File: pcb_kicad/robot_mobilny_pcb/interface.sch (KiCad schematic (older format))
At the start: 21 parts, among them SW3 Button_1

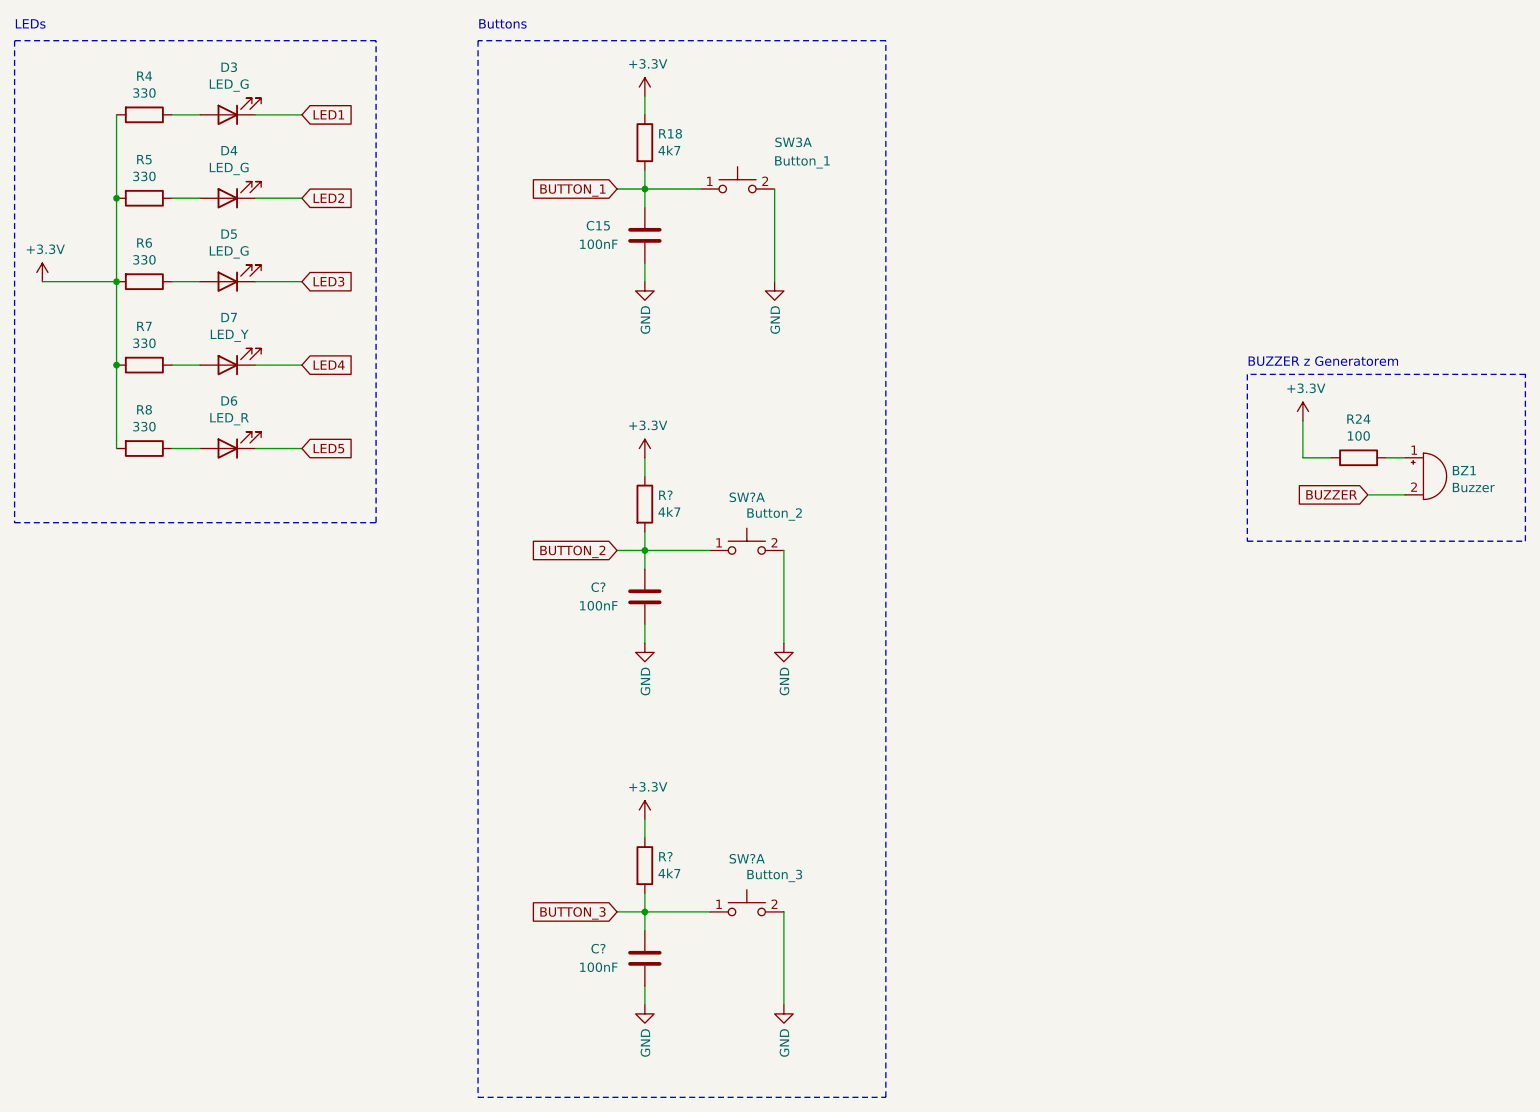
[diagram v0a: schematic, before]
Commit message: schematic update
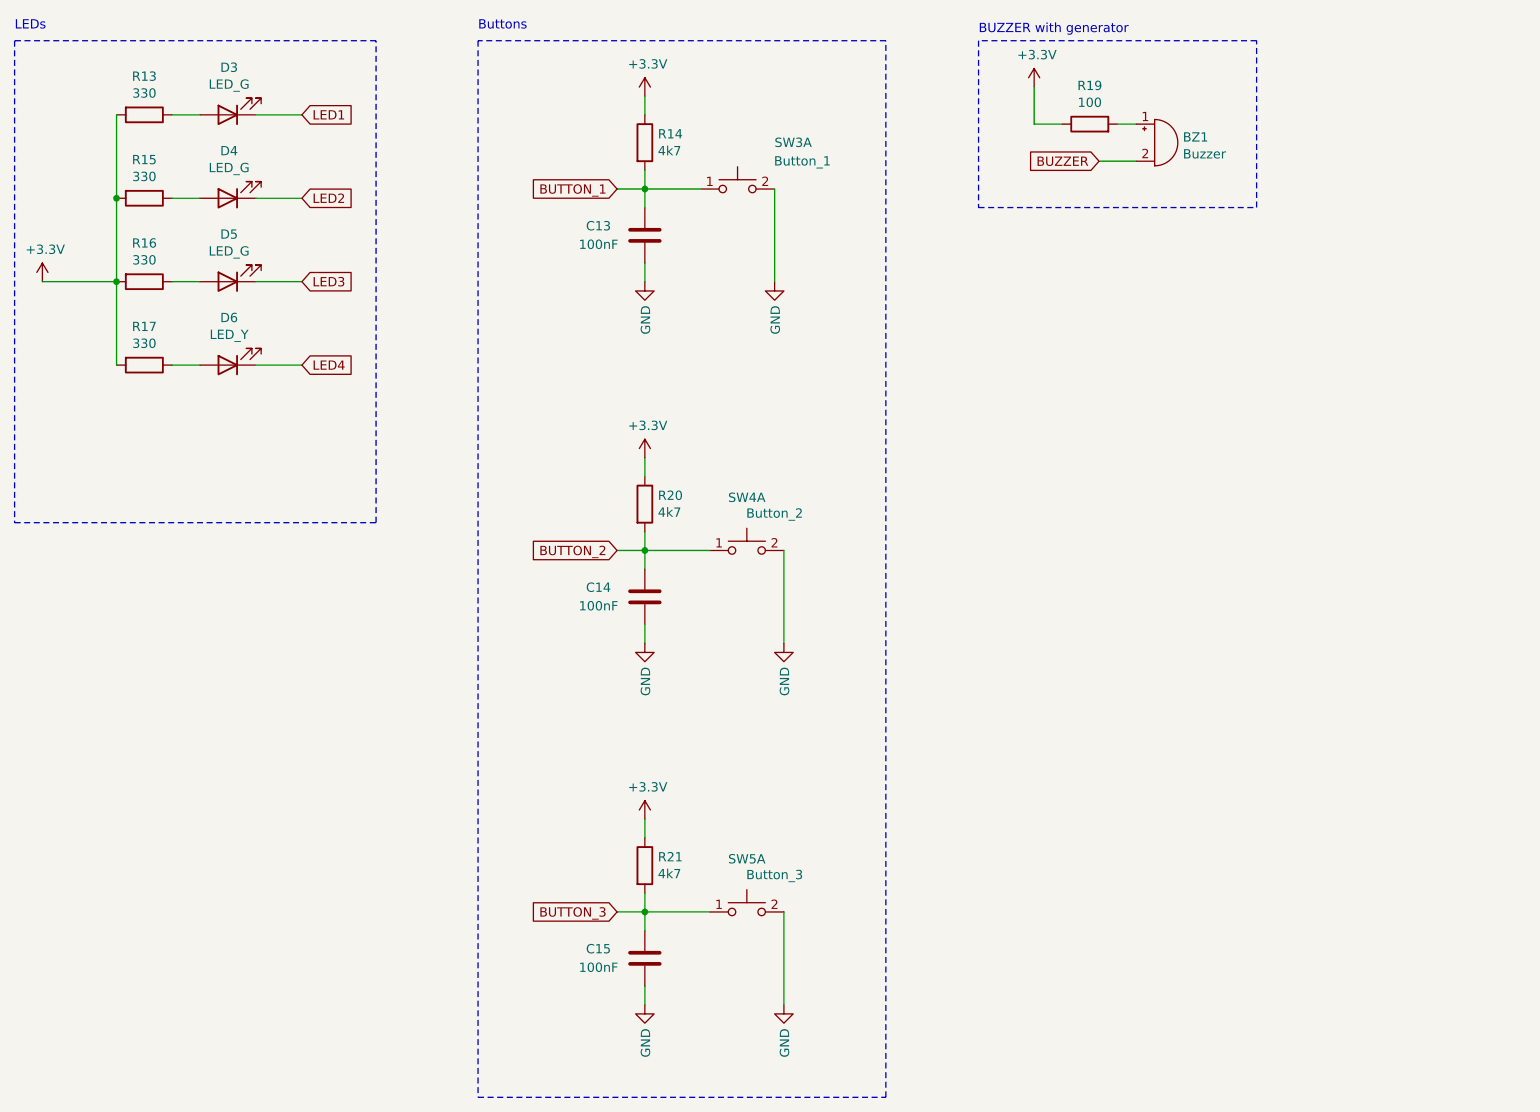
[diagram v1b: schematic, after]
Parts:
- removed D6: LED_R, symbol Device:LED
- removed R8: 330, symbol Device:R
- D3, D4, D5: footprint (none) -> LED_THT:LED_D5.0mm
- D6: renamed from D7; footprint (none) -> LED_THT:LED_D5.0mm
- SW3: footprint (none) -> Button_Switch_THT:SW_PUSH_6mm_H9.5mm
- SW4, SW5: renamed from SW?; footprint (none) -> Button_Switch_THT:SW_PUSH_6mm_H9.5mm
- gave numbers to parts that had none: 4
- renumbered C15 to C13, R4 to R13, R18 to R14, R5 to R15, R6 to R16, R7 to R17, R24 to R19
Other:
- note added: "BUZZER with generator\n\n"
- note removed: "BUZZER z Generatorem\n\n"
- moved on the sheet: BZ1, R19

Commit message: schematic_update
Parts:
- BZ201: renamed from BZ1; footprint (none) -> Buzzer_Beeper:Buzzer_12x9.5RM7.6
- C201: renamed from C13; footprint (none) -> Capacitor_THT:C_Disc_D5.0mm_W2.5mm_P2.50mm
- C202: renamed from C14; footprint (none) -> Capacitor_THT:C_Disc_D5.0mm_W2.5mm_P2.50mm
- C203: renamed from C15; footprint (none) -> Capacitor_THT:C_Disc_D5.0mm_W2.5mm_P2.50mm
- R201: renamed from R13; footprint (none) -> Resistor_THT:R_Axial_DIN0207_L6.3mm_D2.5mm_P10.16mm_Horizontal
- R202: renamed from R19; value 100 -> 330; footprint (none) -> Resistor_THT:R_Axial_DIN0207_L6.3mm_D2.5mm_P10.16mm_Horizontal
- R203: renamed from R14; footprint (none) -> Resistor_THT:R_Axial_DIN0207_L6.3mm_D2.5mm_P10.16mm_Horizontal
- R204: renamed from R15; footprint (none) -> Resistor_THT:R_Axial_DIN0207_L6.3mm_D2.5mm_P10.16mm_Horizontal
- R205: renamed from R16; footprint (none) -> Resistor_THT:R_Axial_DIN0207_L6.3mm_D2.5mm_P10.16mm_Horizontal
- R206: renamed from R17; footprint (none) -> Resistor_THT:R_Axial_DIN0207_L6.3mm_D2.5mm_P10.16mm_Horizontal
- R207: renamed from R20; footprint (none) -> Resistor_THT:R_Axial_DIN0207_L6.3mm_D2.5mm_P10.16mm_Horizontal
- R208: renamed from R21; footprint (none) -> Resistor_THT:R_Axial_DIN0207_L6.3mm_D2.5mm_P10.16mm_Horizontal
- renumbered D3 to D201, D4 to D202, D5 to D203, D6 to D204, SW3 to SW201, SW4 to SW202, SW5 to SW203
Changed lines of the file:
@@
 $EndDescr
 $Comp
-L Device:LED D4
+L Device:LED D202
 U 1 1 617723D4
 P 2600 1950
-F 0 "D4" H 2593 1695 50  0000 C CNN
+F 0 "D202" H 2593 1695 50  0000 C CNN
 F 1 "LED_G" H 2593 1786 50  0000 C CNN
 F 2 "LED_THT:LED_D5.0mm" H 2600 1950 50  0001 C CNN
@@
 $EndComp
 $Comp
-L Device:LED D5
+L Device:LED D203
 U 1 1 61772A27
 P 2600 2400
-F 0 "D5" H 2593 2145 50  0000 C CNN
+F 0 "D203" H 2593 2145 50  0000 C CNN
 F 1 "LED_G" H 2593 2236 50  0000 C CNN
 F 2 "LED_THT:LED_D5.0mm" H 2600 2400 50  0001 C CNN
@@
 $EndComp
 $Comp
-L Device:LED D6
+L Device:LED D204
 U 1 1 61773566
 P 2600 2850
-F 0 "D6" H 2593 2595 50  0000 C CNN
+F 0 "D204" H 2593 2595 50  0000 C CNN
 F 1 "LED_Y" H 2593 2686 50  0000 C CNN
 F 2 "LED_THT:LED_D5.0mm" H 2600 2850 50  0001 C CNN
@@
 $EndComp
 $Comp
-L Device:R R13
+L Device:R R201
 U 1 1 61773BF9
 P 2150 1500
-F 0 "R13" V 1943 1500 50  0000 C CNN
+F 0 "R201" V 1943 1500 50  0000 C CNN
 F 1 "330" V 2034 1500 50  0000 C CNN
-F 2 "" V 2080 1500 50  0001 C CNN
+F 2 "Resistor_THT:R_Axial_DIN0207_L6.3mm_D2.5mm_P10.16mm_Horizontal" V 2080 1500 50  0001 C CNN
 F 3 "~" H 2150 1500 50  0001 C CNN
 	1    2150 1500
@@
 $EndComp
 $Comp
-L Device:R R15
+L Device:R R204
 U 1 1 61774702
 P 2150 1950
-F 0 "R15" V 1943 1950 50  0000 C CNN
+F 0 "R204" V 1943 1950 50  0000 C CNN
 F 1 "330" V 2034 1950 50  0000 C CNN
-F 2 "" V 2080 1950 50  0001 C CNN
+F 2 "Resistor_THT:R_Axial_DIN0207_L6.3mm_D2.5mm_P10.16mm_Horizontal" V 2080 1950 50  0001 C CNN
 F 3 "~" H 2150 1950 50  0001 C CNN
 	1    2150 1950
@@
 $EndComp
 $Comp
-L Device:R R16
+L Device:R R205
 U 1 1 617749A4
 P 2150 2400
-F 0 "R16" V 1943 2400 50  0000 C CNN
+F 0 "R205" V 1943 2400 50  0000 C CNN
 F 1 "330" V 2034 2400 50  0000 C CNN
-F 2 "" V 2080 2400 50  0001 C CNN
+F 2 "Resistor_THT:R_Axial_DIN0207_L6.3mm_D2.5mm_P10.16mm_Horizontal" V 2080 2400 50  0001 C CNN
 F 3 "~" H 2150 2400 50  0001 C CNN
 	1    2150 2400
@@
 $EndComp
 $Comp
-L Device:R R17
+L Device:R R206
 U 1 1 61774CCB
 P 2150 2850
-F 0 "R17" V 1943 2850 50  0000 C CNN
+F 0 "R206" V 1943 2850 50  0000 C CNN
 F 1 "330" V 2034 2850 50  0000 C CNN
-F 2 "" V 2080 2850 50  0001 C CNN
+F 2 "Resistor_THT:R_Axial_DIN0207_L6.3mm_D2.5mm_P10.16mm_Horizontal" V 2080 2850 50  0001 C CNN
 F 3 "~" H 2150 2850 50  0001 C CNN
 	1    2150 2850
@@
 Connection ~ 2000 2400
 $Comp
-L power:+3.3V #PWR028
+L power:+3.3V #PWR0203
 U 1 1 6177600C
 P 1600 2400
-F 0 "#PWR028" H 1600 2250 50  0001 C CNN
+F 0 "#PWR0203" H 1600 2250 50  0001 C CNN
 F 1 "+3.3V" H 1615 2573 50  0000 C CNN
 F 2 "" H 1600 2400 50  0001 C CNN
@@
 	2750 2850 3000 2850
 $Comp
-L Switch:SW_Push_Dual_x2 SW3
+L Switch:SW_Push_Dual_x2 SW201
 U 1 1 6177803B
 P 5350 1900
-F 0 "SW3" H 5650 2150 50  0000 C CNN
+F 0 "SW201" H 5650 2150 50  0000 C CNN
 F 1 "Button_1" H 5700 2050 50  0000 C CNN
 F 2 "Button_Switch_THT:SW_PUSH_6mm_H9.5mm" H 5350 2100 50  0001 C CNN
@@
 $EndComp
 $Comp
-L Device:R R14
+L Device:R R203
 U 1 1 61779C00
 P 4850 1650
-F 0 "R14" H 4920 1696 50  0000 L CNN
+F 0 "R203" H 4920 1696 50  0000 L CNN
 F 1 "4k7" H 4920 1605 50  0000 L CNN
-F 2 "" V 4780 1650 50  0001 C CNN
+F 2 "Resistor_THT:R_Axial_DIN0207_L6.3mm_D2.5mm_P10.16mm_Horizontal" V 4780 1650 50  0001 C CNN
 F 3 "~" H 4850 1650 50  0001 C CNN
 	1    4850 1650
@@
 $EndComp
 $Comp
-L power:+3.3V #PWR027
+L power:+3.3V #PWR0202
 U 1 1 6177B1CB
 P 4850 1400
-F 0 "#PWR027" H 4850 1250 50  0001 C CNN
+F 0 "#PWR0202" H 4850 1250 50  0001 C CNN
 F 1 "+3.3V" H 4865 1573 50  0000 C CNN
 F 2 "" H 4850 1400 50  0001 C CNN
@@
 	4850 1800 4850 1900
 $Comp
-L Device:C C13
+L Device:C C201
 U 1 1 6177C94D
 P 4850 2150
-F 0 "C13" H 5100 2100 50  0000 C CNN
+F 0 "C201" H 5100 2100 50  0000 C CNN
 F 1 "100nF" H 5100 2200 50  0000 C CNN
-F 2 "" H 4888 2000 50  0001 C CNN
+F 2 "Capacitor_THT:C_Disc_D5.0mm_W2.5mm_P2.50mm" H 4888 2000 50  0001 C CNN
 F 3 "~" H 4850 2150 50  0001 C CNN
 	1    4850 2150
@@
 BUTTON_1
 $Comp
-L power:GND #PWR029
+L power:GND #PWR0204
 U 1 1 6177E65E
 P 4850 2400
-F 0 "#PWR029" H 4850 2150 50  0001 C CNN
+F 0 "#PWR0204" H 4850 2150 50  0001 C CNN
 F 1 "GND" V 4855 2272 50  0000 R CNN
 F 2 "" H 4850 2400 50  0001 C CNN
@@
 $EndComp
 $Comp
-L Device:Buzzer BZ1
+L Device:Buzzer BZ201
 U 1 1 61784492
 P 7600 1650
-F 0 "BZ1" H 7752 1679 50  0000 L CNN
+F 0 "BZ201" H 7752 1679 50  0000 L CNN
 F 1 "Buzzer" H 7752 1588 50  0000 L CNN
-F 2 "" V 7575 1750 50  0001 C CNN
+F 2 "Buzzer_Beeper:Buzzer_12x9.5RM7.6" V 7575 1750 50  0001 C CNN
 F 3 "~" V 7575 1750 50  0001 C CNN
 	1    7600 1650
@@
 $EndComp
 $Comp
-L power:+3.3V #PWR031
+L power:+3.3V #PWR0201
 U 1 1 618AE479
 P 6950 1350
-F 0 "#PWR031" H 6950 1200 50  0001 C CNN
+F 0 "#PWR0201" H 6950 1200 50  0001 C CNN
 F 1 "+3.3V" H 6965 1523 50  0000 C CNN
 F 2 "" H 6950 1350 50  0001 C CNN
@@
 	7300 1750 7500 1750
 $Comp
-L Device:R R19
+L Device:R R202
 U 1 1 618B52DF
 P 7250 1550
-F 0 "R19" V 7457 1550 50  0000 C CNN
-F 1 "100" V 7366 1550 50  0000 C CNN
-F 2 "" V 7180 1550 50  0001 C CNN
+F 0 "R202" V 7457 1550 50  0000 C CNN
+F 1 "330" V 7366 1550 50  0000 C CNN
+F 2 "Resistor_THT:R_Axial_DIN0207_L6.3mm_D2.5mm_P10.16mm_Horizontal" V 7180 1550 50  0001 C CNN
 F 3 "~" H 7250 1550 50  0001 C CNN
 	1    7250 1550
@@
 	3400 1100 1450 1100
 $Comp
-L Device:LED D3
+L Device:LED D201
 U 1 1 61771269
 P 2600 1500
-F 0 "D3" H 2593 1245 50  0000 C CNN
+F 0 "D201" H 2593 1245 50  0000 C CNN
 F 1 "LED_G" H 2593 1336 50  0000 C CNN
 F 2 "LED_THT:LED_D5.0mm" H 2600 1500 50  0001 C CNN
@@
 	4850 2300 4850 2400
 $Comp
-L power:GND #PWR030
+L power:GND #PWR0205
 U 1 1 618E5535
 P 5550 2400
-F 0 "#PWR030" H 5550 2150 50  0001 C CNN
+F 0 "#PWR0205" H 5550 2150 50  0001 C CNN
 F 1 "GND" V 5555 2272 50  0000 R CNN
 F 2 "" H 5550 2400 50  0001 C CNN
@@
 BUTTON_3
 $Comp
-L Switch:SW_Push_Dual_x2 SW4
+L Switch:SW_Push_Dual_x2 SW202
 U 1 1 618EB4A2
 P 5400 3850
-F 0 "SW4" H 5400 4135 50  0000 C CNN
+F 0 "SW202" H 5400 4135 50  0000 C CNN
 F 1 "Button_2" H 5550 4050 50  0000 C CNN
 F 2 "Button_Switch_THT:SW_PUSH_6mm_H9.5mm" H 5400 4050 50  0001 C CNN
@@
 $EndComp
 $Comp
-L Device:R R20
+L Device:R R207
 U 1 1 618EB4AE
 P 4850 3600
-F 0 "R20" H 4920 3646 50  0000 L CNN
+F 0 "R207" H 4920 3646 50  0000 L CNN
 F 1 "4k7" H 4920 3555 50  0000 L CNN
-F 2 "" V 4780 3600 50  0001 C CNN
+F 2 "Resistor_THT:R_Axial_DIN0207_L6.3mm_D2.5mm_P10.16mm_Horizontal" V 4780 3600 50  0001 C CNN
 F 3 "~" H 4850 3600 50  0001 C CNN
 	1    4850 3600
@@
 $EndComp
 $Comp
-L power:+3.3V #PWR032
+L power:+3.3V #PWR0206
 U 1 1 618EB4B4
 P 4850 3350
-F 0 "#PWR032" H 4850 3200 50  0001 C CNN
+F 0 "#PWR0206" H 4850 3200 50  0001 C CNN
 F 1 "+3.3V" H 4865 3523 50  0000 C CNN
 F 2 "" H 4850 3350 50  0001 C CNN
@@
 	4850 3750 4850 3850
 $Comp
-L Device:C C14
+L Device:C C202
 U 1 1 618EB4BD
 P 4850 4100
-F 0 "C14" H 5100 4050 50  0000 C CNN
+F 0 "C202" H 5100 4050 50  0000 C CNN
 F 1 "100nF" H 5100 4150 50  0000 C CNN
-F 2 "" H 4888 3950 50  0001 C CNN
+F 2 "Capacitor_THT:C_Disc_D5.0mm_W2.5mm_P2.50mm" H 4888 3950 50  0001 C CNN
 F 3 "~" H 4850 4100 50  0001 C CNN
 	1    4850 4100
@@
 $EndComp
 $Comp
-L power:GND #PWR033
+L power:GND #PWR0207
 U 1 1 618EB4C3
 P 4850 4350
-F 0 "#PWR033" H 4850 4100 50  0001 C CNN
+F 0 "#PWR0207" H 4850 4100 50  0001 C CNN
 F 1 "GND" V 4855 4222 50  0000 R CNN
 F 2 "" H 4850 4350 50  0001 C CNN
@@
 	4850 4250 4850 4350
 $Comp
-L power:GND #PWR034
+L power:GND #PWR0208
 U 1 1 618EB4CD
 P 5600 4350
-F 0 "#PWR034" H 5600 4100 50  0001 C CNN
+F 0 "#PWR0208" H 5600 4100 50  0001 C CNN
 F 1 "GND" V 5605 4222 50  0000 R CNN
 F 2 "" H 5600 4350 50  0001 C CNN
@@
 	5600 3850 5600 4350
 $Comp
-L Switch:SW_Push_Dual_x2 SW5
+L Switch:SW_Push_Dual_x2 SW203
 U 1 1 618EF7CF
 P 5400 5800
-F 0 "SW5" H 5400 6085 50  0000 C CNN
+F 0 "SW203" H 5400 6085 50  0000 C CNN
 F 1 "Button_3" H 5550 6000 50  0000 C CNN
 F 2 "Button_Switch_THT:SW_PUSH_6mm_H9.5mm" H 5400 6000 50  0001 C CNN
@@
 $EndComp
 $Comp
-L Device:R R21
+L Device:R R208
 U 1 1 618EF7DB
 P 4850 5550
-F 0 "R21" H 4920 5596 50  0000 L CNN
+F 0 "R208" H 4920 5596 50  0000 L CNN
 F 1 "4k7" H 4920 5505 50  0000 L CNN
-F 2 "" V 4780 5550 50  0001 C CNN
+F 2 "Resistor_THT:R_Axial_DIN0207_L6.3mm_D2.5mm_P10.16mm_Horizontal" V 4780 5550 50  0001 C CNN
 F 3 "~" H 4850 5550 50  0001 C CNN
 	1    4850 5550
@@
 $EndComp
 $Comp
-L power:+3.3V #PWR035
+L power:+3.3V #PWR0209
 U 1 1 618EF7E1
 P 4850 5300
-F 0 "#PWR035" H 4850 5150 50  0001 C CNN
+F 0 "#PWR0209" H 4850 5150 50  0001 C CNN
 F 1 "+3.3V" H 4865 5473 50  0000 C CNN
 F 2 "" H 4850 5300 50  0001 C CNN
@@
 	4850 5700 4850 5800
 $Comp
-L Device:C C15
+L Device:C C203
 U 1 1 618EF7EA
 P 4850 6050
-F 0 "C15" H 5100 6000 50  0000 C CNN
+F 0 "C203" H 5100 6000 50  0000 C CNN
 F 1 "100nF" H 5100 6100 50  0000 C CNN
-F 2 "" H 4888 5900 50  0001 C CNN
+F 2 "Capacitor_THT:C_Disc_D5.0mm_W2.5mm_P2.50mm" H 4888 5900 50  0001 C CNN
 F 3 "~" H 4850 6050 50  0001 C CNN
 	1    4850 6050
@@
 $EndComp
 $Comp
-L power:GND #PWR036
+L power:GND #PWR0210
 U 1 1 618EF7F0
 P 4850 6300
-F 0 "#PWR036" H 4850 6050 50  0001 C CNN
+F 0 "#PWR0210" H 4850 6050 50  0001 C CNN
 F 1 "GND" V 4855 6172 50  0000 R CNN
 F 2 "" H 4850 6300 50  0001 C CNN
@@
 	4850 6200 4850 6300
 $Comp
-L power:GND #PWR037
+L power:GND #PWR0211
 U 1 1 618EF7FA
 P 5600 6300
-F 0 "#PWR037" H 5600 6050 50  0001 C CNN
+F 0 "#PWR0211" H 5600 6050 50  0001 C CNN
 F 1 "GND" V 5605 6172 50  0000 R CNN
 F 2 "" H 5600 6300 50  0001 C CNN
